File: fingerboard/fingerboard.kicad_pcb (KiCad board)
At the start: 2 copper layers, 15 x 72.5 mm, 8 parts, among them J1 Conn_01x05_Pin, SW1 SW_Push, SW2 SW_Push, SW3 SW_Push, SW4 SW_Push

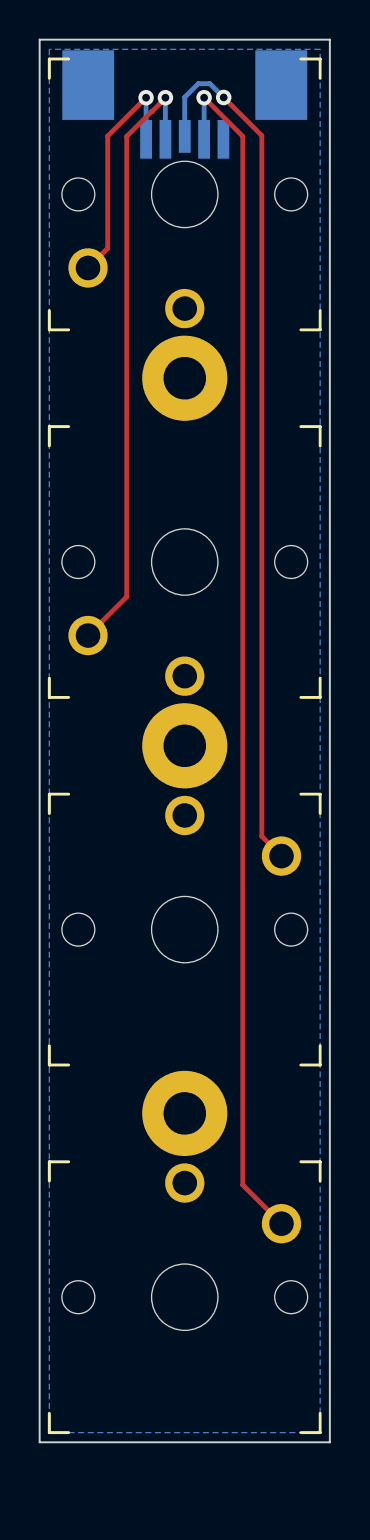
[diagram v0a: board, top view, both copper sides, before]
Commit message: small tweaks, incl thumbboard side springs (and fabrication frame)
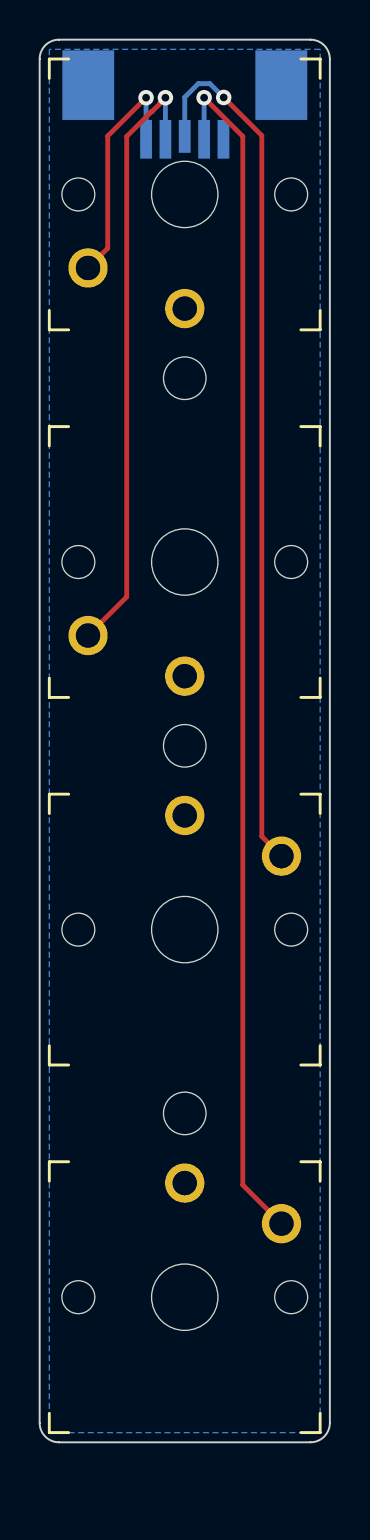
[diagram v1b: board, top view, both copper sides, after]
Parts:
- removed H1, H2, H3: MountingHole, MountingHole:MountingHole_2.2mm_M2_Pad
- added REF**: NPTH 2.2mm, panelization:NPTH 2.2mm, F.Cu at (157.5, 87.5)
- added REF**: NPTH 2.2mm, panelization:NPTH 2.2mm, F.Cu at (157.5, 49.5)
- added REF**: NPTH 2.2mm, panelization:NPTH 2.2mm, F.Cu at (157.5, 68.5)
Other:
- outline, holes or cut-outs redrawn
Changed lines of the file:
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@@
   (net 5 "Row4")
   (net 6 "unconnected-(J1-MountPin-PadMP)")
+  (footprint "panelization:NPTH 2.2mm" (layer "F.Cu")
+    (at 157.5 87.5)
+    (attr board_only)
+    (fp_text reference "REF**" (at 0 -0.5 unlocked) (layer "F.SilkS") hide
+        (effects (font (size 1 1) (thickness 0.1)))
+    )
+    (fp_text value "NPTH 2.2mm" (at 0 1 unlocked) (layer "F.Fab")
+        (effects (font (size 1 1) (thickness 0.15)))
+    )
+    (fp_text user "${REFERENCE}" (at 0 2.5 unlocked) (layer "F.Fab")
+        (effects (font (size 1 1) (thickness 0.15)))
+    )
+    (pad "" np_thru_hole circle (at 0 0) (size 0.0001 0.0001) (drill 2.2) (layers "F&B.Cu"))
+  )
+  (footprint "panelization:NPTH 2.2mm" (layer "F.Cu")
+    (at 157.5 49.5)
+    (attr board_only)
+    (fp_text reference "REF**" (at 0 -0.5 unlocked) (layer "F.SilkS") hide
+        (effects (font (size 1 1) (thickness 0.1)))
+    )
+    (fp_text value "NPTH 2.2mm" (at 0 1 unlocked) (layer "F.Fab")
+        (effects (font (size 1 1) (thickness 0.15)))
+    )
+    (pad "" np_thru_hole circle (at 0 0) (size 0.0001 0.0001) (drill 2.2) (layers "F&B.Cu"))
+  )
   (footprint "keyswitches:SW_PG1350" (layer "F.Cu")
     (at 157.5 97 180)
@@
       (net 2 "Row1") (pinfunction "2") (pintype "passive"))
   )
-  (footprint "MountingHole:MountingHole_2.2mm_M2_Pad" (layer "F.Cu")
-    (at 157.5 87.5)
-    (descr "Mounting Hole 2.2mm, M2")
-    (tags "mounting hole 2.2mm m2")
-    (property "Sheetfile" "fingerboard.kicad_sch")
-    (property "Sheetname" "")
-    (property "ki_description" "Mounting Hole without connection")
-    (property "ki_keywords" "mounting hole")
-    (attr board_only exclude_from_pos_files)
-    (fp_text reference "H3" (at 0 -3.2) (layer "F.SilkS") hide
-        (effects (font (size 1 1) (thickness 0.15)))
-    )
-    (fp_text value "MountingHole" (at 0 3.2) (layer "F.Fab") hide
-        (effects (font (size 1 1) (thickness 0.15)))
-    )
-    (fp_text user "${REFERENCE}" (at 0 0) (layer "F.Fab") hide
-        (effects (font (size 1 1) (thickness 0.15)))
-    )
-    (fp_circle (center 0 0) (end 2.2 0)
-      (stroke (width 0.15) (type solid)) (fill none) (layer "Cmts.User"))
-    (fp_circle (center 0 0) (end 2.45 0)
-      (stroke (width 0.05) (type solid)) (fill none) (layer "F.CrtYd"))
-    (pad "1" thru_hole circle (at 0 0) (size 4.4 4.4) (drill 2.2) (layers "*.Cu" "*.Mask"))
-  )
-  (footprint "MountingHole:MountingHole_2.2mm_M2_Pad" (layer "F.Cu")
-    (at 157.5 68.5)
-    (descr "Mounting Hole 2.2mm, M2")
-    (tags "mounting hole 2.2mm m2")
-    (property "Sheetfile" "fingerboard.kicad_sch")
-    (property "Sheetname" "")
-    (property "ki_description" "Mounting Hole without connection")
-    (property "ki_keywords" "mounting hole")
-    (attr board_only exclude_from_pos_files)
-    (fp_text reference "H2" (at 0 -3.2) (layer "F.SilkS") hide
-        (effects (font (size 1 1) (thickness 0.15)))
-    )
-    (fp_text value "MountingHole" (at 0 3.2) (layer "F.Fab") hide
-        (effects (font (size 1 1) (thickness 0.15)))
-    )
-    (fp_text user "${REFERENCE}" (at 0 0) (layer "F.Fab") hide
-        (effects (font (size 1 1) (thickness 0.15)))
-    )
-    (fp_circle (center 0 0) (end 2.2 0)
-      (stroke (width 0.15) (type solid)) (fill none) (layer "Cmts.User"))
-    (fp_circle (center 0 0) (end 2.45 0)
-      (stroke (width 0.05) (type solid)) (fill none) (layer "F.CrtYd"))
-    (pad "1" thru_hole circle (at 0 0) (size 4.4 4.4) (drill 2.2) (layers "*.Cu" "*.Mask"))
-  )
   (footprint "keyswitches:SW_PG1350" (layer "F.Cu")
     (at 157.5 78 180)
@@
       (net 4 "Row3") (pinfunction "2") (pintype "passive"))
   )
-  (footprint "MountingHole:MountingHole_2.2mm_M2_Pad" (layer "F.Cu")
-    (at 157.5 49.5)
-    (descr "Mounting Hole 2.2mm, M2")
-    (tags "mounting hole 2.2mm m2")
-    (property "Sheetfile" "fingerboard.kicad_sch")
-    (property "Sheetname" "")
-    (property "ki_description" "Mounting Hole without connection")
-    (property "ki_keywords" "mounting hole")
-    (attr board_only exclude_from_pos_files)
-    (fp_text reference "H1" (at 0 -3.2) (layer "F.SilkS") hide
-        (effects (font (size 1 1) (thickness 0.15)))
-    )
-    (fp_text value "MountingHole" (at 0 3.2) (layer "F.Fab") hide
-        (effects (font (size 1 1) (thickness 0.15)))
-    )
-    (fp_text user "${REFERENCE}" (at 0 0) (layer "F.Fab") hide
-        (effects (font (size 1 1) (thickness 0.15)))
-    )
-    (fp_circle (center 0 0) (end 2.2 0)
-      (stroke (width 0.15) (type solid)) (fill none) (layer "Cmts.User"))
-    (fp_circle (center 0 0) (end 2.45 0)
-      (stroke (width 0.05) (type solid)) (fill none) (layer "F.CrtYd"))
-    (pad "1" thru_hole circle (at 0 0) (size 4.4 4.4) (drill 2.2) (layers "*.Cu" "*.Mask"))
+  (footprint "panelization:NPTH 2.2mm" (layer "F.Cu")
+    (at 157.5 68.5)
+    (attr board_only)
+    (fp_text reference "REF**" (at 0 -0.5 unlocked) (layer "F.SilkS") hide
+        (effects (font (size 1 1) (thickness 0.1)))
+    )
+    (fp_text value "NPTH 2.2mm" (at 0 1 unlocked) (layer "F.Fab")
+        (effects (font (size 1 1) (thickness 0.15)))
+    )
+    (pad "" np_thru_hole circle (at 0 0) (size 0.0001 0.0001) (drill 2.2) (layers "F&B.Cu"))
   )
   (footprint "keyswitches:SW_PG1350" (layer "F.Cu")
@@
     )
   )
-  (gr_rect (start 150 32) (end 165 104.5)
-    (stroke (width 0.1) (type default)) (fill none) (layer "Edge.Cuts"))
+  (gr_arc (start 164 32) (mid 164.707107 32.292893) (end 165 33)
+    (stroke (width 0.1) (type default)) (layer "Edge.Cuts"))
+  (gr_line (start 164 104.5) (end 151 104.5)
+    (stroke (width 0.1) (type default)) (layer "Edge.Cuts"))
+  (gr_arc (start 150 33) (mid 150.292893 32.292893) (end 151 32)
+    (stroke (width 0.1) (type default)) (layer "Edge.Cuts"))
+  (gr_arc (start 151 104.5) (mid 150.292893 104.207107) (end 150 103.5)
+    (stroke (width 0.1) (type default)) (layer "Edge.Cuts"))
+  (gr_arc (start 165 103.5) (mid 164.707107 104.207107) (end 164 104.5)
+    (stroke (width 0.1) (type default)) (layer "Edge.Cuts"))
+  (gr_line (start 165 33) (end 165 103.5)
+    (stroke (width 0.1) (type default)) (layer "Edge.Cuts"))
+  (gr_line (start 150 103.5) (end 150 33)
+    (stroke (width 0.1) (type default)) (layer "Edge.Cuts"))
+  (gr_line (start 151 32) (end 164 32)
+    (stroke (width 0.1) (type default)) (layer "Edge.Cuts"))
   (dimension (type orthogonal) (layer "User.7")
     (pts (xy 160.5 80) (xy 160 90))
@@
   )
   (dimension (type orthogonal) (layer "User.7")
-    (pts (xy 166 32) (xy 166.5 28.5))
-    (height 7.5)
-    (orientation 1)
-    (gr_text "3.5000 mm" (at 172.35 30.25 90) (layer "User.7")
+    (pts (xy 150 104.5) (xy 165 104.5))
+    (height 14.5)
+    (orientation 0)
+    (gr_text "15.0000 mm" (at 157.5 117.85) (layer "User.7")
       (effects (font (size 1 1) (thickness 0.15)))
     )
@@
   )
   (dimension (type orthogonal) (layer "User.7")
-    (pts (xy 149 28.5) (xy 149 104.5))
+    (pts (xy 149 32) (xy 149 104.5))
     (height -17.5)
     (orientation 1)
-    (gr_text "76.0000 mm" (at 130.35 66.5 90) (layer "User.7")
-      (effects (font (size 1 1) (thickness 0.15)))
-    )
+    (gr_text "72.5000 mm" (at 130.35 68.25 90) (layer "User.7")
+      (effects (font (size 1 1) (thickness 0.15)))
+    )

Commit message: change base key pitch from 19mm to 20mm
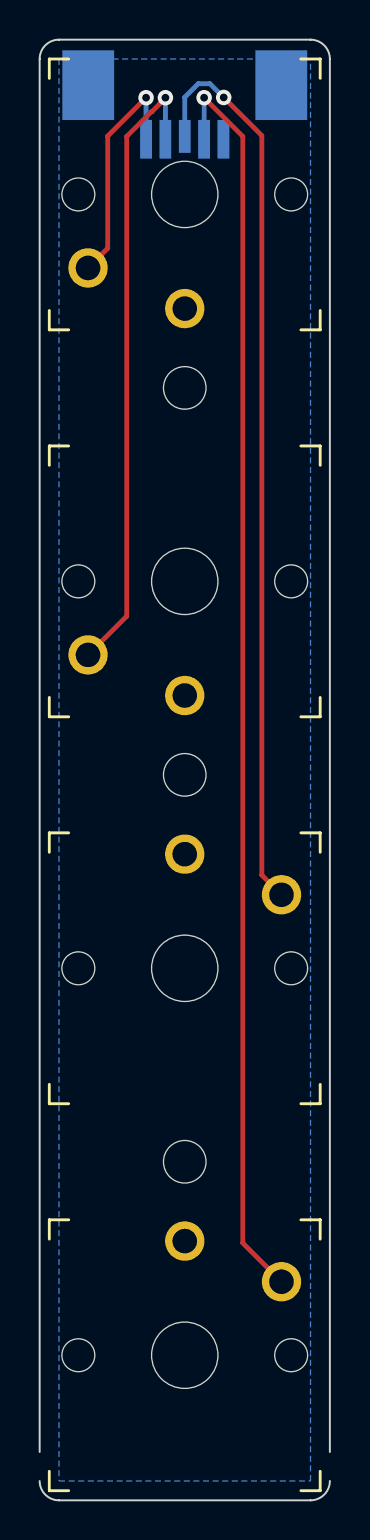
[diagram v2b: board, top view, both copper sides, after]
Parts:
- moved SW4 3.00 mm to (157.5, 100.0)
- moved REF** 2.50 mm to (157.5, 90.0)
- moved SW3 2.00 mm to (157.5, 80.0)
- moved REF** 1.50 mm to (157.5, 70.0)
- moved SW2 1.00 mm to (157.5, 60.0)
- moved REF** 0.50 mm to (157.5, 50.0)
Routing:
- net Row4: track 62.0 -> 65.0 mm
- net Row3: track 45.2 -> 47.2 mm
- net Row2: track 31.6 -> 32.6 mm
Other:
- board size 15 x 72.5 mm -> 15 x 75.5 mm
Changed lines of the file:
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@@
   (net 6 "unconnected-(J1-MountPin-PadMP)")
   (footprint "panelization:NPTH 2.2mm" (layer "F.Cu")
-    (at 157.5 87.5)
+    (at 157.5 90)
     (attr board_only)
     (fp_text reference "REF**" (at 0 -0.5 unlocked) (layer "F.SilkS") hide
@@
   )
   (footprint "panelization:NPTH 2.2mm" (layer "F.Cu")
-    (at 157.5 49.5)
+    (at 157.5 50)
     (attr board_only)
     (fp_text reference "REF**" (at 0 -0.5 unlocked) (layer "F.SilkS") hide
@@
   )
   (footprint "keyswitches:SW_PG1350" (layer "F.Cu")
-    (at 157.5 97 180)
+    (at 157.5 100 180)
     (descr "Kailh \"Choc\" PG1350 keyswitch")
     (tags "kailh,choc")
@@
   )
   (footprint "keyswitches:SW_PG1350" (layer "F.Cu")
-    (at 157.5 78 180)
+    (at 157.5 80 180)
     (descr "Kailh \"Choc\" PG1350 keyswitch")
     (tags "kailh,choc")
@@
   )
   (footprint "panelization:NPTH 2.2mm" (layer "F.Cu")
-    (at 157.5 68.5)
+    (at 157.5 70)
     (attr board_only)
     (fp_text reference "REF**" (at 0 -0.5 unlocked) (layer "F.SilkS") hide
@@
   )
   (footprint "keyswitches:SW_PG1350" (layer "F.Cu")
-    (at 157.5 59)
+    (at 157.5 60)
     (descr "Kailh \"Choc\" PG1350 keyswitch")
     (tags "kailh,choc")
@@
   (gr_arc (start 164 32) (mid 164.707107 32.292893) (end 165 33)
     (stroke (width 0.1) (type default)) (layer "Edge.Cuts"))
-  (gr_line (start 164 104.5) (end 151 104.5)
+  (gr_line (start 164 107.5) (end 151 107.5)
     (stroke (width 0.1) (type default)) (layer "Edge.Cuts"))
   (gr_arc (start 150 33) (mid 150.292893 32.292893) (end 151 32)
     (stroke (width 0.1) (type default)) (layer "Edge.Cuts"))
-  (gr_arc (start 151 104.5) (mid 150.292893 104.207107) (end 150 103.5)
-    (stroke (width 0.1) (type default)) (layer "Edge.Cuts"))
-  (gr_arc (start 165 103.5) (mid 164.707107 104.207107) (end 164 104.5)
-    (stroke (width 0.1) (type default)) (layer "Edge.Cuts"))
-  (gr_line (start 165 33) (end 165 103.5)
-    (stroke (width 0.1) (type default)) (layer "Edge.Cuts"))
-  (gr_line (start 150 103.5) (end 150 33)
+  (gr_arc (start 151 107.5) (mid 150.292893 107.207107) (end 150 106.5)
+    (stroke (width 0.1) (type default)) (layer "Edge.Cuts"))
+  (gr_arc (start 165 106.5) (mid 164.707107 107.207107) (end 164 107.5)
+    (stroke (width 0.1) (type default)) (layer "Edge.Cuts"))
+  (gr_line (start 165 33) (end 165 105)
+    (stroke (width 0.1) (type default)) (layer "Edge.Cuts"))
+  (gr_line (start 150 105) (end 150 33)
     (stroke (width 0.1) (type default)) (layer "Edge.Cuts"))
   (gr_line (start 151 32) (end 164 32)
     (stroke (width 0.1) (type default)) (layer "Edge.Cuts"))
   (dimension (type orthogonal) (layer "User.7")
-    (pts (xy 160.5 80) (xy 160 90))
+    (pts (xy 160.5 82) (xy 160 93))
     (height 19.5)
     (orientation 1)
-    (gr_text "10.0000 mm" (at 178.85 85 90) (layer "User.7")
-      (effects (font (size 1 1) (thickness 0.15)))
-    )
-    (format (prefix "") (suffix "") (units 3) (units_format 1) (precision 4))
-    (style (thickness 0.15) (arrow_length 1.27) (text_position_mode 0) (extension_height 0.58642) (extension_offset 0.5) keep_text_aligned)
-  )
-  (dimension (type orthogonal) (layer "User.7")
-    (pts (xy 159.5 99) (xy 159.5 104.5))
+    (gr_text "11.0000 mm" (at 178.85 88 90) (layer "User.7")
+      (effects (font (size 1 1) (thickness 0.15)))
+    )
+    (format (prefix "") (suffix "") (units 3) (units_format 1) (precision 4))
+    (style (thickness 0.15) (arrow_length 1.27) (text_position_mode 2) (extension_height 0.58642) (extension_offset 0.5) keep_text_aligned)
+  )
+  (dimension (type orthogonal) (layer "User.7")
+    (pts (xy 159.5 102) (xy 159.5 107.5))
     (height 20.5)
     (orientation 1)
-    (gr_text "5.5000 mm" (at 178.85 101.75 90) (layer "User.7")
+    (gr_text "5.5000 mm" (at 178.85 104.75 90) (layer "User.7")
       (effects (font (size 1 1) (thickness 0.15)))
     )
@@
   )
   (dimension (type orthogonal) (layer "User.7")
-    (pts (xy 166 71) (xy 158 80))
+    (pts (xy 166 73) (xy 158 82))
     (height 7.5)
     (orientation 1)
-    (gr_text "9.0000 mm" (at 172.35 75.5 90) (layer "User.7")
-      (effects (font (size 1 1) (thickness 0.15)))
-    )
-    (format (prefix "") (suffix "") (units 3) (units_format 1) (precision 4))
-    (style (thickness 0.15) (arrow_length 1.27) (text_position_mode 0) (extension_height 0.58642) (extension_offset 0.5) keep_text_aligned)
-  )
-  (dimension (type orthogonal) (layer "User.7")
-    (pts (xy 162 47) (xy 158 57))
+    (gr_text "9.0000 mm" (at 172.35 77.5 90) (layer "User.7")
+      (effects (font (size 1 1) (thickness 0.15)))
+    )
+    (format (prefix "") (suffix "") (units 3) (units_format 1) (precision 4))
+    (style (thickness 0.15) (arrow_length 1.27) (text_position_mode 0) (extension_height 0.58642) (extension_offset 0.5) keep_text_aligned)
+  )
+  (dimension (type orthogonal) (layer "User.7")
+    (pts (xy 162 47) (xy 158 58))
     (height 18.5)
     (orientation 1)
-    (gr_text "10.0000 mm" (at 179.35 52 90) (layer "User.7")
+    (gr_text "11.0000 mm" (at 179.35 52.5 90) (layer "User.7")
       (effects (font (size 1 1) (thickness 0.15)))
     )
@@
   )
   (dimension (type orthogonal) (layer "User.7")
-    (pts (xy 161 66) (xy 161 71))
+    (pts (xy 161 67) (xy 161 73))
     (height 19.5)
     (orientation 1)
-    (gr_text "5.0000 mm" (at 179.35 68.5 90) (layer "User.7")
-      (effects (font (size 1 1) (thickness 0.15)))
-    )
-    (format (prefix "") (suffix "") (units 3) (units_format 1) (precision 4))
-    (style (thickness 0.15) (arrow_length 1.27) (text_position_mode 0) (extension_height 0.58642) (extension_offset 0.5) keep_text_aligned)
-  )
-  (dimension (type orthogonal) (layer "User.7")
-    (pts (xy 160 90) (xy 159.5 99))
+    (gr_text "6.0000 mm" (at 179.35 70 90) (layer "User.7")
+      (effects (font (size 1 1) (thickness 0.15)))
+    )
+    (format (prefix "") (suffix "") (units 3) (units_format 1) (precision 4))
+    (style (thickness 0.15) (arrow_length 1.27) (text_position_mode 0) (extension_height 0.58642) (extension_offset 0.5) keep_text_aligned)
+  )
+  (dimension (type orthogonal) (layer "User.7")
+    (pts (xy 160 93) (xy 159.5 102))
     (height 13.5)
     (orientation 1)
-    (gr_text "9.0000 mm" (at 172.35 94.5 90) (layer "User.7")
+    (gr_text "9.0000 mm" (at 172.35 97.5 90) (layer "User.7")
       (effects (font (size 1 1) (thickness 0.15)))
     )
@@
   )
   (dimension (type orthogonal) (layer "User.7")
-    (pts (xy 166 57) (xy 167 66))
+    (pts (xy 166 58) (xy 167 67))
     (height 7.5)
     (orientation 1)
-    (gr_text "9.0000 mm" (at 172.35 61.5 90) (layer "User.7")
+    (gr_text "9.0000 mm" (at 172.35 62.5 90) (layer "User.7")
       (effects (font (size 1 1) (thickness 0.15)))
     )
@@
   (via (at 155.5 35) (size 0.8) (drill 0.4) (layers "F.Cu" "B.Cu") (net 2))
   (segment (start 155.5 35) (end 155.5 37.15) (width 0.25) (layer "B.Cu") (net 2))
+  (segment (start 155.775 35.725) (end 155.800305 35.725) (width 0.25) (layer "F.Cu") (net 3))
+  (segment (start 154.5 61.8) (end 154.5 37) (width 0.25) (layer "F.Cu") (net 3))
   (segment (start 156.225 35.300305) (end 156.225 35.275) (width 0.25) (layer "F.Cu") (net 3))
   (segment (start 156.225 35.275) (end 156.5 35) (width 0.25) (layer "F.Cu") (net 3))
-  (segment (start 154.5 60.8) (end 154.5 37) (width 0.25) (layer "F.Cu") (net 3))
-  (segment (start 155.775 35.725) (end 155.800305 35.725) (width 0.25) (layer "F.Cu") (net 3))
   (segment (start 155.800305 35.725) (end 156.225 35.300305) (width 0.25) (layer "F.Cu") (net 3))
   (segment (start 154.5 37) (end 155.775 35.725) (width 0.25) (layer "F.Cu") (net 3))
-  (segment (start 152.5 62.8) (end 154.5 60.8) (width 0.25) (layer "F.Cu") (net 3))
+  (segment (start 152.5 63.8) (end 154.5 61.8) (width 0.25) (layer "F.Cu") (net 3))
   (via (at 156.5 35) (size 0.8) (drill 0.4) (layers "F.Cu" "B.Cu") (net 3))
   (segment (start 156.5 35) (end 156.5 37.15) (width 0.25) (layer "B.Cu") (net 3))
+  (segment (start 161.484001 75.184001) (end 161.484001 36.959403) (width 0.25) (layer "F.Cu") (net 4))
+  (segment (start 162.5 76.2) (end 161.484001 75.184001) (width 0.25) (layer "F.Cu") (net 4))
   (segment (start 161.484001 36.959403) (end 159.512299 34.987701) (width 0.25) (layer "F.Cu") (net 4))
-  (segment (start 162.5 74.2) (end 161.484001 73.184001) (width 0.25) (layer "F.Cu") (net 4))
-  (segment (start 161.484001 73.184001) (end 161.484001 36.959403) (width 0.25) (layer "F.Cu") (net 4))
   (via (at 159.512299 34.987701) (size 0.8) (drill 0.4) (layers "F.Cu" "B.Cu") (net 4))
   (segment (start 158.799598 34.275) (end 158.199695 34.275) (width 0.25) (layer "B.Cu") (net 4))
@@
   (segment (start 159.512299 34.987701) (end 158.799598 34.275) (width 0.25) (layer "B.Cu") (net 4))
   (segment (start 158.199695 34.275) (end 157.5 34.974695) (width 0.25) (layer "B.Cu") (net 4))
-  (segment (start 160.5 37) (end 160.5 91.2) (width 0.25) (layer "F.Cu") (net 5))
-  (segment (start 160.5 91.2) (end 162.5 93.2) (width 0.25) (layer "F.Cu") (net 5))
-  (segment (start 158.5 35) (end 160.5 37) (width 0.25) (layer "F.Cu") (net 5))
+  (segment (start 162.5 96.2) (end 160.5 94.2) (width 0.25) (layer "F.Cu") (net 5))
+  (segment (start 160.5 37) (end 158.5 35) (width 0.25) (layer "F.Cu") (net 5))
+  (segment (start 160.5 94.2) (end 160.5 37) (width 0.25) (layer "F.Cu") (net 5))
   (via (at 158.5 35) (size 0.8) (drill 0.4) (layers "F.Cu" "B.Cu") (net 5))
   (segment (start 158.5 37.15) (end 158.5 35) (width 0.25) (layer "B.Cu") (net 5))
@@
     (polygon
       (pts
-        (xy 150.5 32.5)
-        (xy 150.5 104)
-        (xy 164.5 104)
-        (xy 164.5 32.5)
+        (xy 151 33)
+        (xy 151 106.5)
+        (xy 164 106.5)
+        (xy 164 33)
       )
     )
